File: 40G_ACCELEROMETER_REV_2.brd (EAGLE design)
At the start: 18.8 x 24.1 mm, 30 parts, among them IC1 3.3V_LDO, IC2 X_BUFFER, IC3 Y_BUFFER, IC4 Z_BUFFER

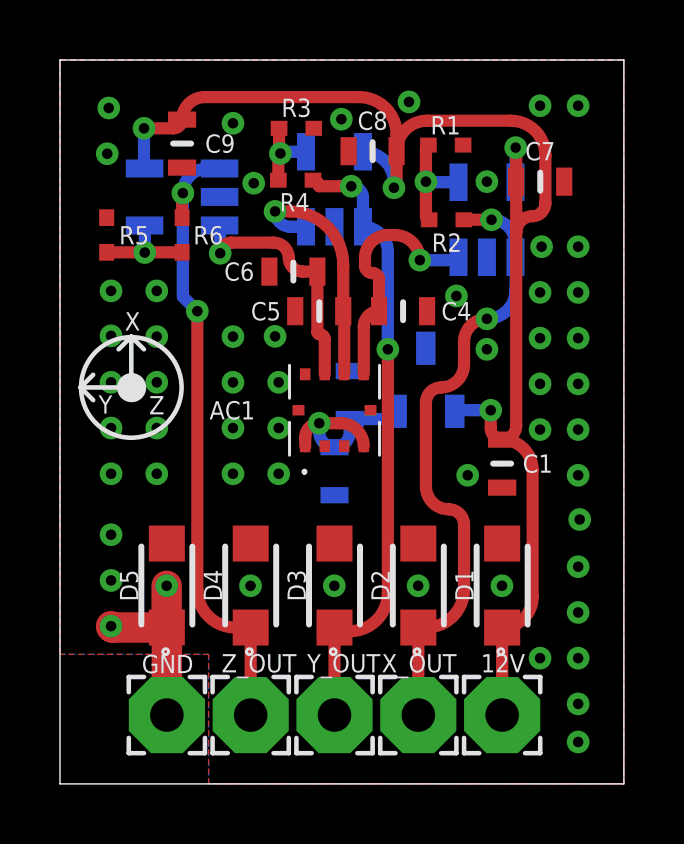
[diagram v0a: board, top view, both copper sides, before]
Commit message: Changed LDO input cap and LDO to parts that are in stock.
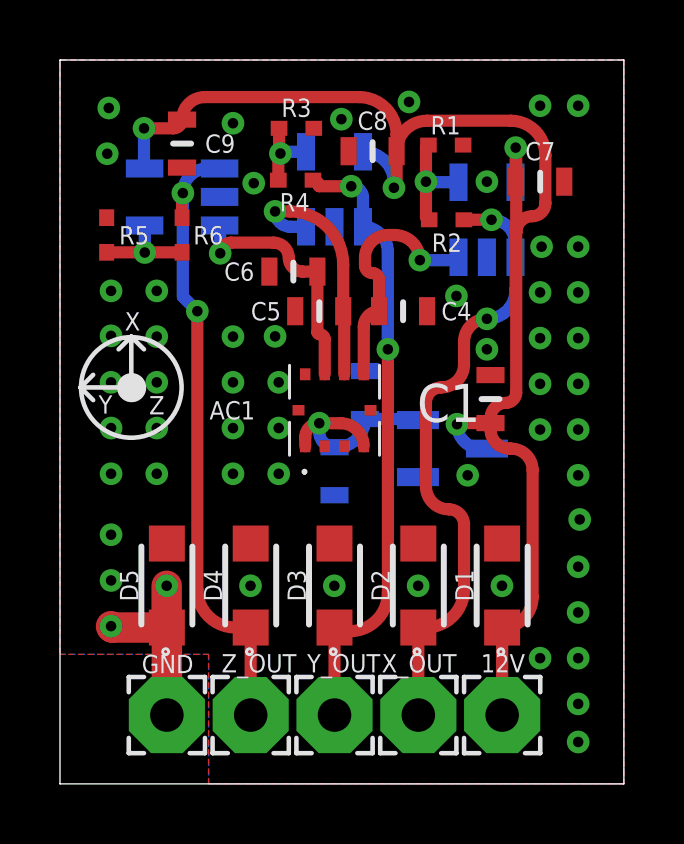
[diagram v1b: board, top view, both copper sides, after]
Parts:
- C1: value 1uF -> 2.2uF
- IC1: value 3.3V_LDO -> MCP1792T-3302H_CB; device SamacSys_Parts:SOT96P240X110-3N -> SamacSys_Parts:SOT95P255X145-3N
- moved IC1 2.46 mm to (13.1, 11.2), turned to 180 degrees
- moved C1 2.19 mm to (14.4, 12.8), turned to 90 degrees
- moved C2 0.51 mm to (10.2, 13.0)
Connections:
- net 12V: now also IC1.3; no longer IC1.1
- net GND: now also IC1.1; no longer IC1.3
